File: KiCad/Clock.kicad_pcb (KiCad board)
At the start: 2 copper layers, 75 x 105 mm, 77 parts, among them J1 USB_C_Receptacle_USB2.0, J2 SWD, J3 DISP, J4 BASE, Q1 PMV75UP, Q2 PMV75UP, Q3 PMV65UN, Q4 PMV65UN, Q5 PMV65UN, Q6 PMV65UN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

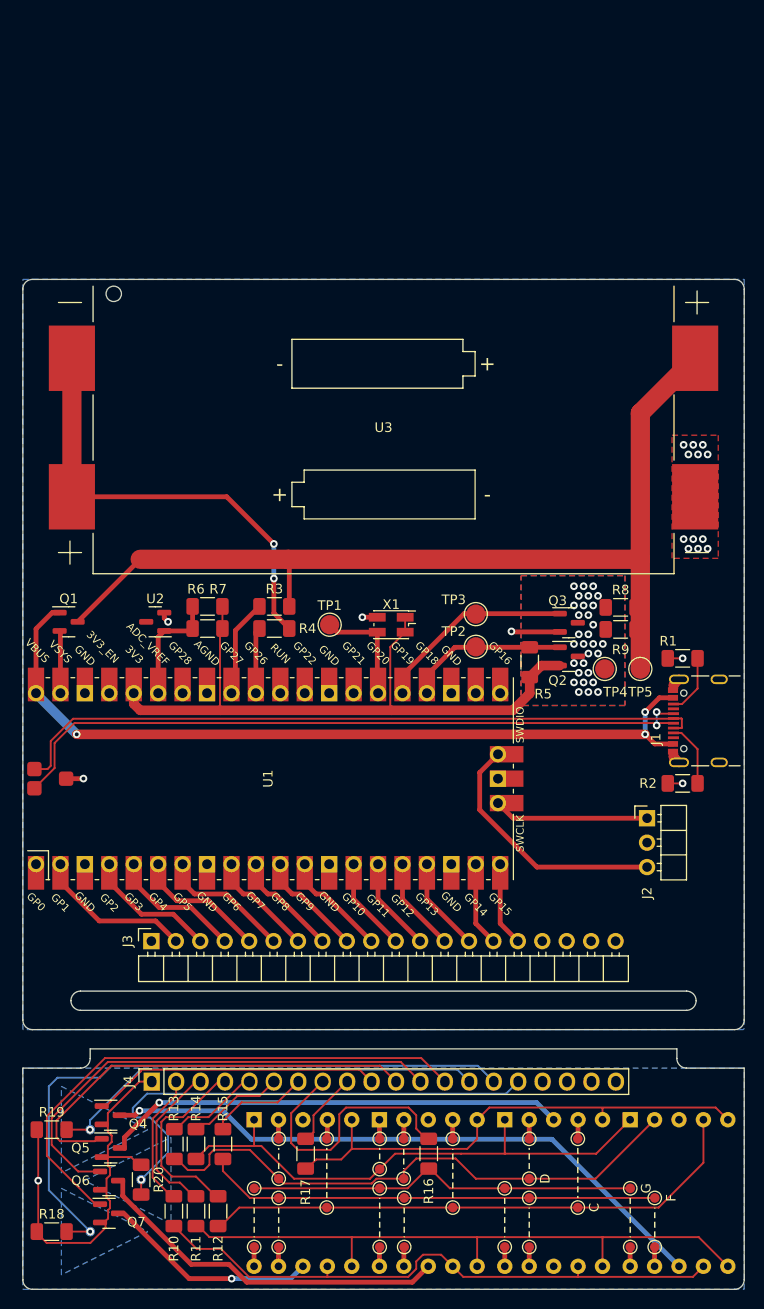
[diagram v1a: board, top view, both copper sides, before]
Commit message: Adjust the PCB for fabrication
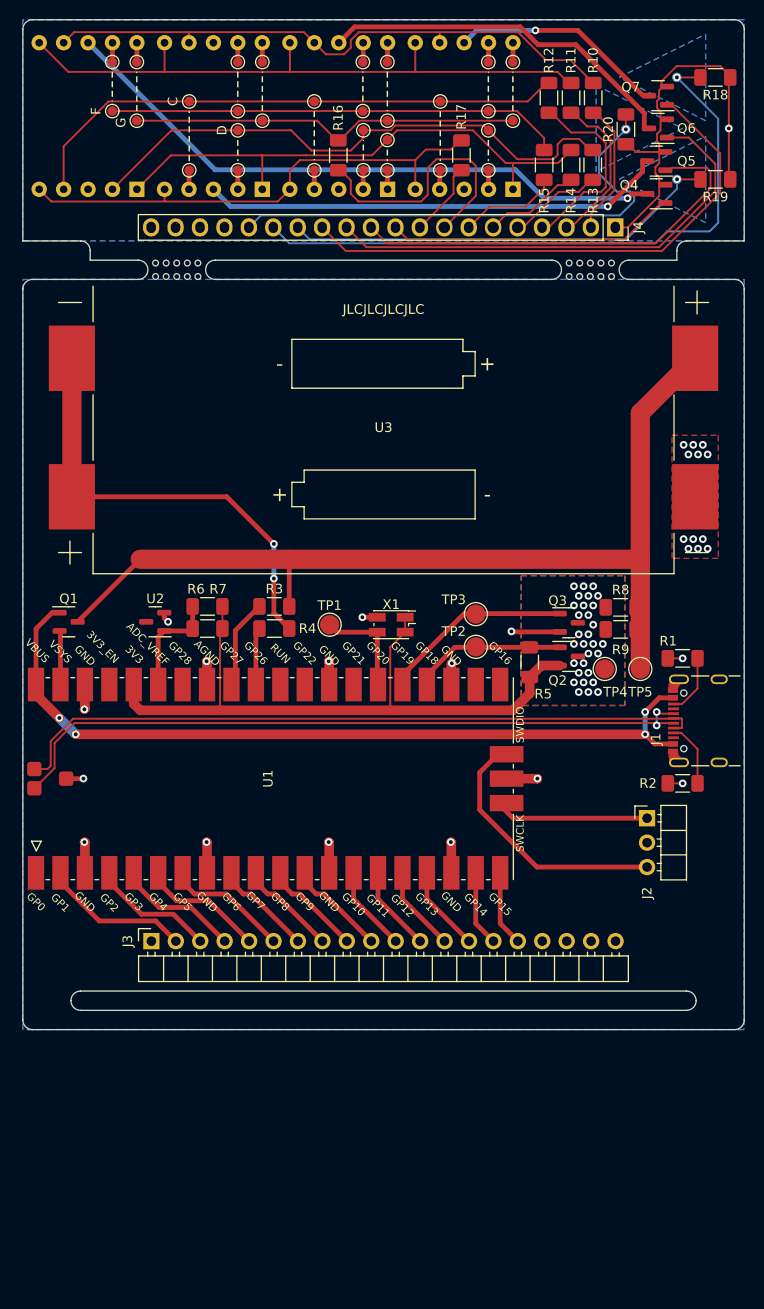
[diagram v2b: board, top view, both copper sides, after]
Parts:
- added H1: Mouse Bites, Custom:MouseBites_2x05mm, F.Cu at (46.0, 28.0)
- added H2: Mouse Bites, Custom:MouseBites_2x05mm, F.Cu at (89.0, 28.0)
- added SYM1: Logo_Open_Hardware_Small, Symbol:OSHW-Logo2_24.3x20mm_SilkScreen, B.Cu at (67.5, 44.4)
- U1: footprint RPi_Pico:RPi_Pico_SMD_TH -> RPi_Pico:RPi_Pico_SMD
- moved R18 138.4 mm to (102.0, 8.00), turned to 180 degrees
- moved TP_F5 135.5 mm to (39.3, 6.40), turned to 180 degrees
- moved TP6 134.6 mm to (98.0, 8.00), turned to 0 degrees
- moved TP_G5 133.5 mm to (41.9, 6.40), turned to 180 degrees
- moved Q7 129.5 mm to (96.0, 9.90), turned to 180 degrees
- moved TP_F6 126.9 mm to (52.4, 6.40), turned to 180 degrees
- moved TP_F4 126.3 mm to (39.3, 11.5), turned to 180 degrees
- moved TP_G8 126.1 mm to (81.0, 6.40), turned to 180 degrees
- moved TP_G6 125.8 mm to (54.9, 6.40), turned to 180 degrees
- moved TP_F8 125.1 mm to (78.4, 6.40), turned to 180 degrees
- moved R10 123.7 mm to (89.3, 10.1), turned to -90 degrees
- moved Q6 123.4 mm to (96.0, 13.3), turned to 180 degrees
- moved TP_F7 123.3 mm to (65.3, 6.40), turned to 180 degrees
- moved TP_G7 123.2 mm to (67.9, 6.40), turned to 180 degrees
- moved TP_G4 122.3 mm to (41.9, 12.5), turned to 180 degrees
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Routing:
- net GND: track 57.3 -> 82.2 mm, vias 19 -> 28
- net /VBUS: track 84.2 -> 84.3 mm, vias 3 -> 4
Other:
- outline, holes or cut-outs redrawn
- board text added: "JLCJLCJLCJLC"
